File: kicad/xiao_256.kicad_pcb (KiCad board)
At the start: 2 copper layers, 64 parts, among them J1 Conn_01x02_Pin, J2 Conn_01x02_Pin, SW1 GateronLP, SW10 GateronLP, SW11 GateronLP, SW12 GateronLP, SW13 GateronLP, SW14 GateronLP, SW15 GateronLP, SW16 GateronLP, SW17 GateronLP, SW18 GateronLP, SW19 GateronLP, SW2 GateronLP, SW20 GateronLP, SW21 GateronLP, SW22 GateronLP, SW23 GateronLP, SW24 GateronLP, SW25 GateronLP, SW26 GateronLP, SW27 GateronLP, SW28 GateronLP, SW29 GateronLP, SW3 GateronLP, SW30 GateronLP, SW4 GateronLP, SW5 GateronLP, SW6 GateronLP, SW7 GateronLP, SW8 GateronLP, SW9 GateronLP, U1 Seeed XIAO, U2 SK12D07VG4

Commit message: finish routing
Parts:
- added H1: Hole_Pad, xiao_256:Mount_M2, F.Cu at (39.6, 39.5)
- added H2: Hole_Pad, xiao_256:Mount_M2, F.Cu at (39.5, 96.5)
- added H3: Hole_Pad, xiao_256:Mount_M2, F.Cu at (140.0, 45.5)
- added H4: Hole_Pad, xiao_256:Mount_M2, F.Cu at (140.0, 110.0)
- added H5: Hole_Pad, xiao_256:Mount_M2, F.Cu at (154.0, 45.5)
- added H6: Hole_Pad, xiao_256:Mount_M2, F.Cu at (154.0, 110.0)
- moved U2 4.74 mm to (152.5, 53.5)
- moved J1 4.61 mm to (142.0, 51.5)
- moved J2 4.61 mm to (147.0, 51.5)
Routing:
- net COL3: track 142.7 -> 214.9 mm
- net ROW5: track 207.7 -> 198.3 mm
- net COL5: track 182.2 -> 172.9 mm
- net ROW4: track 186.2 -> 178.4 mm
- net COL1: track 251.9 -> 257.3 mm
- net COL4: track 198.9 -> 193.9 mm
- net COL6: track 156.7 -> 152.0 mm
- net COL2: track 233.0 -> 235.8 mm
- net ROW2: track 126.0 -> 128.1 mm
- net CHGR+: track 12.2 -> 11.7 mm
- net BATT+: track 6.83 -> 6.33 mm
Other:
- board outline added: 137.2 x 95.5 mm

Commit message: gerber, not done yet
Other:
- board size 137.2 x 95.5 mm -> 137.5 x 96 mm
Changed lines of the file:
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@@
     (pad_to_mask_clearance 0)
     (pcbplotparams
-      (layerselection 0x00010fc_ffffffff)
+      (layerselection 0x00010cc_ffffffff)
       (plot_on_all_layers_selection 0x0000000_00000000)
       (disableapertmacros false)
-      (usegerberextensions false)
-      (usegerberattributes true)
-      (usegerberadvancedattributes true)
-      (creategerberjobfile true)
+      (usegerberextensions true)
+      (usegerberattributes false)
+      (usegerberadvancedattributes false)
+      (creategerberjobfile false)
       (dashed_line_dash_ratio 12.000000)
       (dashed_line_gap_ratio 3.000000)
@@
       (plotinvisibletext false)
       (sketchpadsonfab false)
-      (subtractmaskfromsilk false)
+      (subtractmaskfromsilk true)
       (outputformat 1)
       (mirror false)
-      (drillshape 1)
+      (drillshape 0)
       (scaleselection 1)
-      (outputdirectory "")
+      (outputdirectory "../gerber/")
     )
   )
@@
     (property "Sheetname" "")
     (attr through_hole)
-    (fp_text reference "U2" (at 0 0 90) (layer "F.SilkS")
+    (fp_text reference "U2" (at 0 0 90) (layer "F.SilkS") hide
         (effects (font (size 0.787402 0.787402) (thickness 0.15)))
     )
-    (fp_text value "SK12D07VG4" (at 0 0 90) (layer "F.Fab")
+    (fp_text value "SK12D07VG4" (at 0 0 90) (layer "F.Fab") hide
         (effects (font (size 0.787402 0.787402) (thickness 0.15)))
     )
@@
     (property "Sheetname" "")
     (attr through_hole)
-    (fp_text reference "U1" (at 0 -0.5 unlocked) (layer "F.SilkS")
+    (fp_text reference "U1" (at 0 -0.5 unlocked) (layer "F.SilkS") hide
         (effects (font (size 1 1) (thickness 0.1)))
     )
@@
     )
   )
-  (gr_arc (start 22.25 116) (mid 20.835786 115.414214) (end 20.25 114)
+  (gr_arc (start 157.5 114) (mid 156.914214 115.414214) (end 155.5 116)
     (stroke (width 0.1) (type default)) (layer "Edge.Cuts"))
-  (gr_line (start 20.25 114) (end 20.25 22.5)
+  (gr_line (start 155.5 116) (end 22 116)
     (stroke (width 0.1) (type default)) (layer "Edge.Cuts"))
-  (gr_arc (start 20.25 22.5) (mid 20.835786 21.085786) (end 22.25 20.5)
+  (gr_line (start 157.5 22) (end 157.5 114)
     (stroke (width 0.1) (type default)) (layer "Edge.Cuts"))
-  (gr_line (start 157.5 22.5) (end 157.5 114)
+  (gr_line (start 20 114) (end 20 22)
     (stroke (width 0.1) (type default)) (layer "Edge.Cuts"))
-  (gr_arc (start 155.5 20.5) (mid 156.914214 21.085786) (end 157.5 22.5)
+  (gr_arc (start 155.5 20) (mid 156.914214 20.585786) (end 157.5 22)
     (stroke (width 0.1) (type default)) (layer "Edge.Cuts"))
-  (gr_line (start 155.5 116) (end 22.25 116)
+  (gr_arc (start 22 116) (mid 20.585786 115.414214) (end 20 114)
     (stroke (width 0.1) (type default)) (layer "Edge.Cuts"))
-  (gr_line (start 22.25 20.5) (end 155.5 20.5)
+  (gr_arc (start 20 22) (mid 20.585786 20.585786) (end 22 20)
     (stroke (width 0.1) (type default)) (layer "Edge.Cuts"))
-  (gr_arc (start 157.5 114) (mid 156.914214 115.414214) (end 155.5 116)
+  (gr_line (start 22 20) (end 155.5 20)
     (stroke (width 0.1) (type default)) (layer "Edge.Cuts"))
   (segment (start 154.24 24.264255) (end 141.49456 24.264255) (width 0.25) (layer "F.Cu") (net 1))

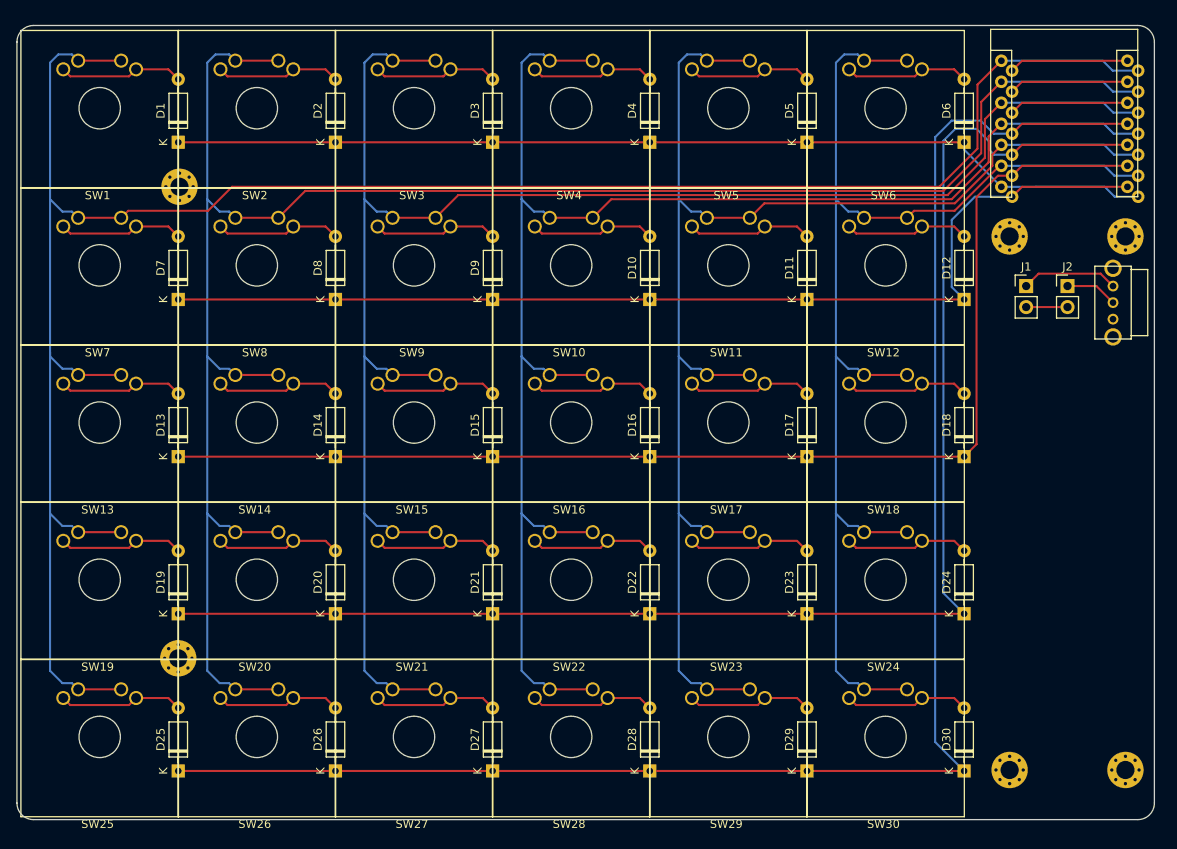
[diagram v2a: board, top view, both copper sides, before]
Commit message: add cover, tweak footprints
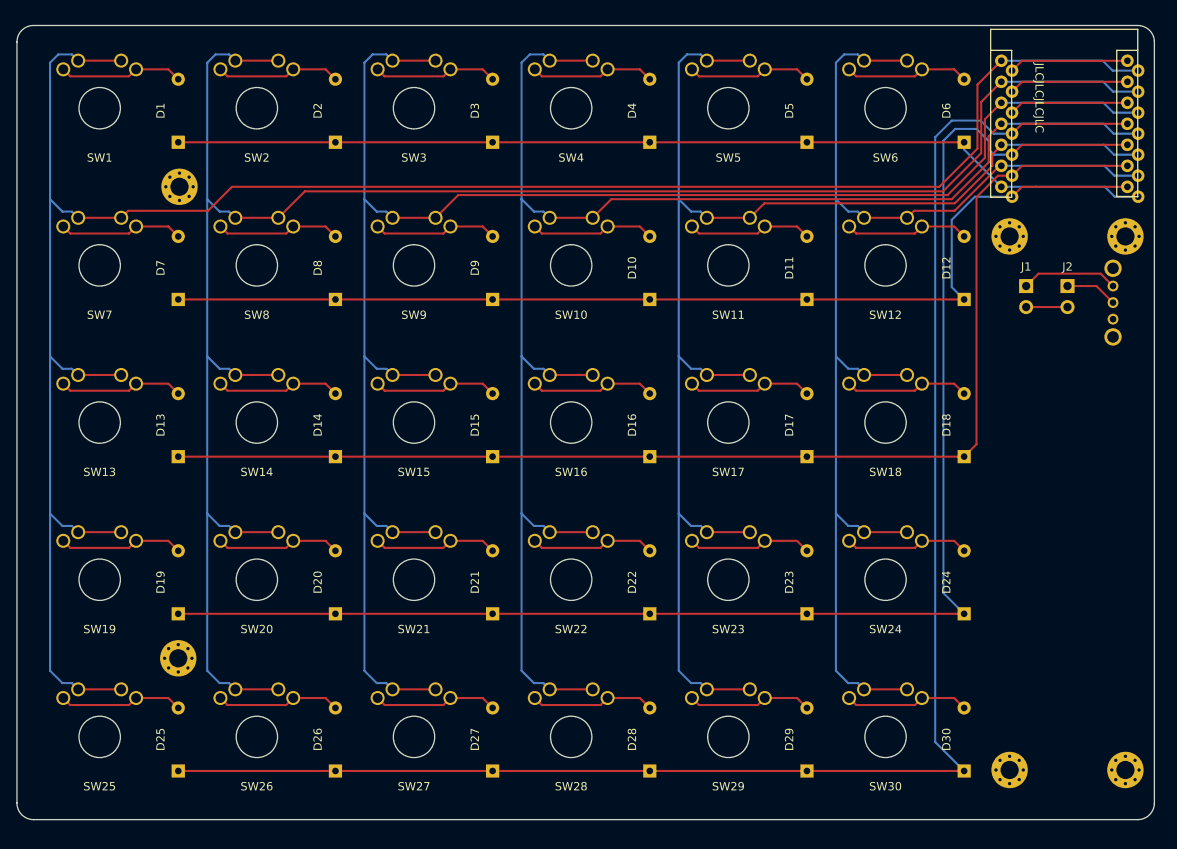
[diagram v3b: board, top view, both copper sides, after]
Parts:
- D1, D10, D11, D12, D13, D14, D15, D16, D17, D18, D19, D2, D20, D21, D22, D23, D24, D25, D26, D27, D28, D29, D3, D30, D4, D5, D6, D7, D8, D9: footprint Diode_THT:D_DO-35_SOD27_P7.62mm_Horizontal -> xiao_256:D_DO-35_SOD27_P7.62mm_Horizontal
- J1, J2: footprint Connector_PinHeader_2.54mm:PinHeader_1x02_P2.54mm_Vertical -> xiao_256:PinHeader_1x02_P2.54mm_Vertical
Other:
- board text added: "JLCJLCJLCJLC"
